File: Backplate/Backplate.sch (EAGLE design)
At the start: 28 parts, among them J1 USB_FTP, Q1 BQ2970, Q2 CSD16406Q3, Q3 CSD16406Q3, X1 Batt/Sun, X3 USB

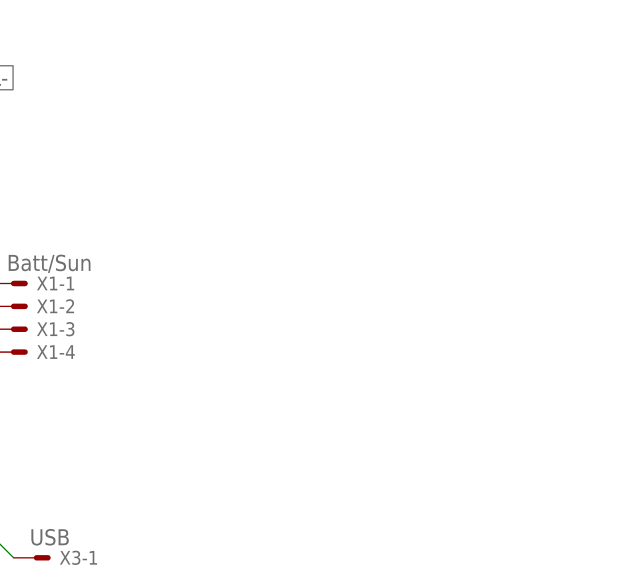
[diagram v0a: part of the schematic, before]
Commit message: Backplate v1.1 ordered
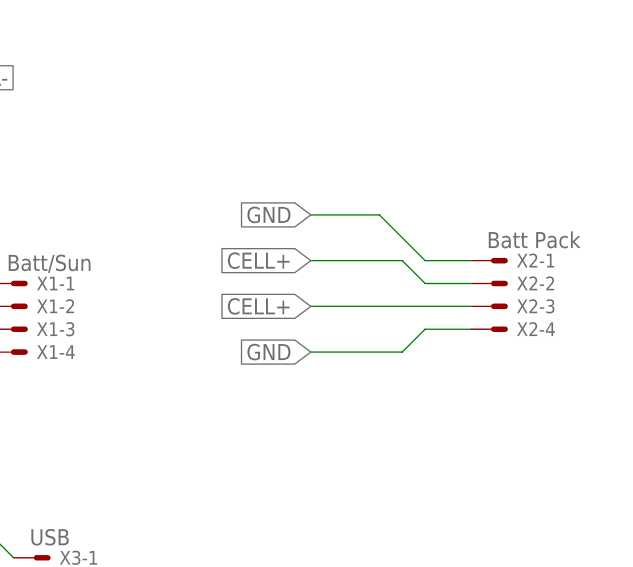
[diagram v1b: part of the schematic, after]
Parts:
- added X2: Batt Pack, con-molex:22-23-2041
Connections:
- net CELL+: now also X2-2.S, X2-3.S
- net GND: now also X2-1.S, X2-4.S
